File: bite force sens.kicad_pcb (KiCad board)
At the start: 2 copper layers, 47.5 x 50 mm, 31 parts, among them J1 lipo bat, J2 tp4056 pin, J3 tp4056 pin, J4 fsr, J5 display, SW1 on/off, SW2 reset, U1 MCP6004, U2 MCP1700-3302E_TO, U3 ESP32-C3-WROOM-02-N4

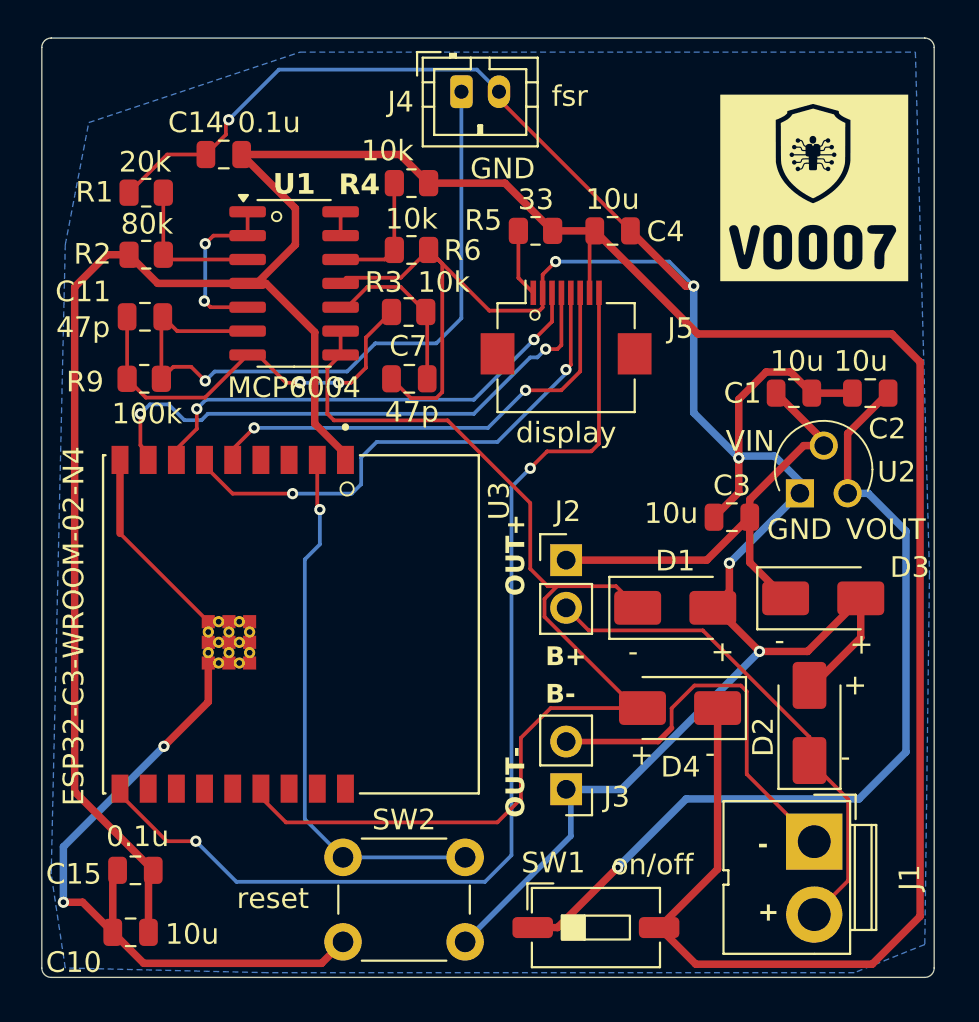
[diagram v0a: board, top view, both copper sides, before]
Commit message: Changed the pcb to 4layer since the mcu is used and this is just the model without looking for the SI/PI,EMC/EMI
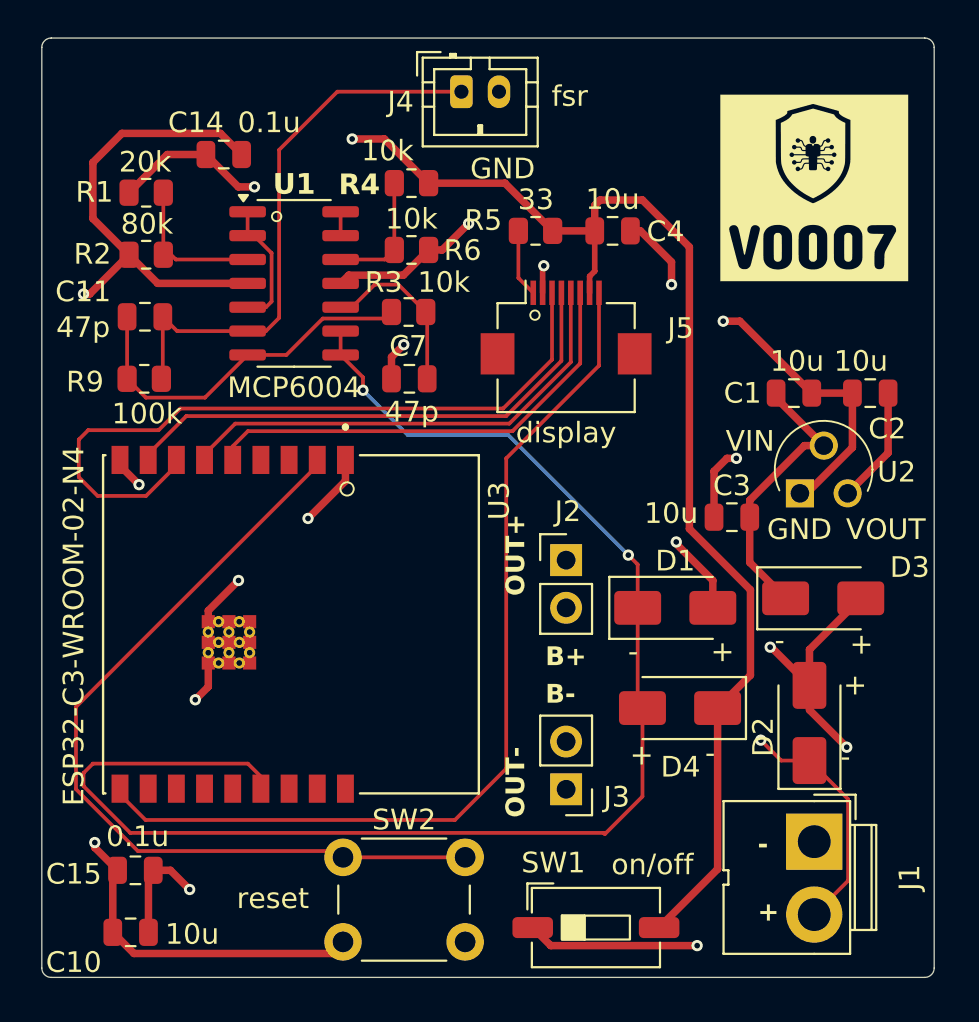
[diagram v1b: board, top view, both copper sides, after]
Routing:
- net /3v3: track 170.6 -> 202.7 mm, vias 0 -> 4
- net /en: track 28.9 -> 45.1 mm, vias 1 -> 0
- net /V3: track 62.4 -> 77.5 mm, vias 0 -> 2
- net /RESET: track 25.5 -> 39.1 mm, vias 2 -> 0
- net GND: track 195.9 -> 186.0 mm, vias 8 -> 14
- net Net-(J4-Pin_1): track 38.1 -> 30.1 mm, vias 1 -> 0
- net /CS: track 56.9 -> 49.9 mm, vias 2 -> 0
- net /v: track 25.7 -> 31.9 mm
- net /-: track 20.8 -> 15.4 mm
- net /3.3: track 45.7 -> 50.8 mm
- net /SDA: track 28.0 -> 25.5 mm, vias 2 -> 0
- net /v1: track 9.22 -> 6.91 mm, vias 2 -> 0
- net /v2: track 21.8 -> 19.7 mm, vias 2 -> 0
- net /RS: track 30.0 -> 28.0 mm, vias 2 -> 0
- net /+: track 26.8 -> 28.1 mm, vias 0 -> 1
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- added copper zone on In2.Cu, net /3v3
- added copper zone on In1.Cu, net GND
- removed copper zone on B.Cu, net GND
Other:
- copper layers 2 -> 4
- board text removed: "0.1500 mm / 0.1500 mm"
- board text removed: "0.3000 mm"
- board text removed: "1.6000 mm"
- board text removed: "2"
- board text removed: "47.5000 mm x 50.0000 mm"
- board text removed: "BOARD CHARACTERISTICS"
- board text removed: "Board Thickness:"
- board text removed: "Board overall dimensions:"
- board text removed: "Castellated pads:"
- board text removed: "Copper Finish:"
- board text removed: "Copper Layer Count:"
- board text removed: "Edge card connectors:"
- board text removed: "Impedance Control:"
- board text removed: "Min hole diameter:"
- board text removed: "Min track/spacing:"
- board text removed: "No"
- board text removed: "None"
- board text removed: "Plated Board Edge:"
